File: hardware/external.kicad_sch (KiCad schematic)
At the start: 10 parts, among them J4 Conn_02x04_Odd_Even, J8 Conn_01x04_Pin, J9 Conn_01x04_Pin

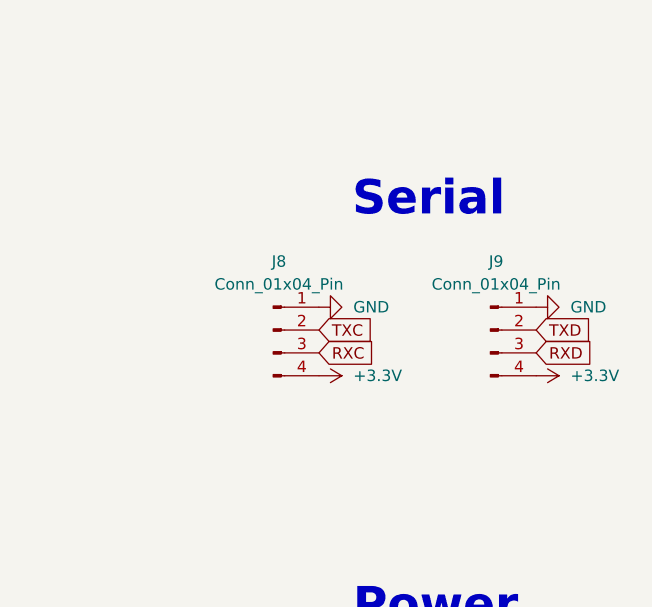
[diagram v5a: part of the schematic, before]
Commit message: Add new categories for Video&Audio and Sound System in project configuration
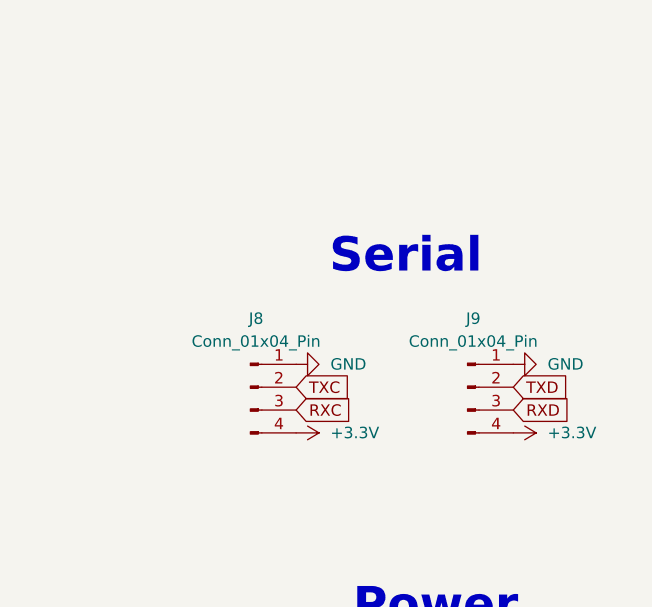
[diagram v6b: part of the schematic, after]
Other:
- moved on the sheet: J8, J9
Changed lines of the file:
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@@
 	(text "Serial\n"
 		(exclude_from_sim no)
-		(at 224.282 79.502 0)
+		(at 221.742 85.852 0)
 		(effects
 			(font
@@
 	(global_label "RXC"
 		(shape input)
-		(at 212.09 96.52 0)
+		(at 209.55 102.87 0)
 		(fields_autoplaced yes)
 		(effects
@@
 		)
 		(property "Intersheetrefs" "${INTERSHEET_REFS}"
-			(at 218.8247 96.52 0)
+			(at 216.2847 102.87 0)
 			(effects
 				(font
@@
 	(global_label "TXC"
 		(shape input)
-		(at 212.09 93.98 0)
+		(at 209.55 100.33 0)
 		(fields_autoplaced yes)
 		(effects
@@
 		)
 		(property "Intersheetrefs" "${INTERSHEET_REFS}"
-			(at 218.5223 93.98 0)
+			(at 215.9823 100.33 0)
 			(effects
 				(font
@@
 	(global_label "TXD"
 		(shape input)
-		(at 236.22 93.98 0)
+		(at 233.68 100.33 0)
 		(fields_autoplaced yes)
 		(effects
@@
 		)
 		(property "Intersheetrefs" "${INTERSHEET_REFS}"
-			(at 242.6523 93.98 0)
+			(at 240.1123 100.33 0)
 			(effects
 				(font
@@
 	(global_label "RXD"
 		(shape input)
-		(at 236.22 96.52 0)
+		(at 233.68 102.87 0)
 		(fields_autoplaced yes)
 		(effects
@@
 		)
 		(property "Intersheetrefs" "${INTERSHEET_REFS}"
-			(at 242.9547 96.52 0)
+			(at 240.4147 102.87 0)
 			(effects
 				(font
@@
 	(symbol
 		(lib_id "Connector:Conn_01x04_Pin")
-		(at 231.14 93.98 0)
+		(at 228.6 100.33 0)
 		(unit 1)
 		(exclude_from_sim no)
@@
 		(fields_autoplaced yes)
 		(property "Reference" "J9"
-			(at 231.775 86.36 0)
+			(at 229.235 92.71 0)
 			(effects
 				(font
@@
 		)
 		(property "Value" "Conn_01x04_Pin"
-			(at 231.775 88.9 0)
+			(at 229.235 95.25 0)
 			(effects
 				(font
@@
 		)
 		(property "Footprint" "Connector_PinHeader_2.54mm:PinHeader_1x04_P2.54mm_Vertical"
-			(at 231.14 93.98 0)
+			(at 228.6 100.33 0)
 			(effects
 				(font
@@
 		)
 		(property "Datasheet" "~"
-			(at 231.14 93.98 0)
+			(at 228.6 100.33 0)
 			(effects
 				(font
@@
 		)
 		(property "Description" "Generic connector, single row, 01x04, script generated"
-			(at 231.14 93.98 0)
+			(at 228.6 100.33 0)
 			(effects
 				(font
@@
 	(symbol
 		(lib_id "Connector:Conn_01x04_Pin")
-		(at 207.01 93.98 0)
+		(at 204.47 100.33 0)
 		(unit 1)
 		(exclude_from_sim no)
@@
 		(fields_autoplaced yes)
 		(property "Reference" "J8"
-			(at 207.645 86.36 0)
+			(at 205.105 92.71 0)
 			(effects
 				(font
@@
 		)
 		(property "Value" "Conn_01x04_Pin"
-			(at 207.645 88.9 0)
+			(at 205.105 95.25 0)
 			(effects
 				(font
@@
 		)
 		(property "Footprint" "Connector_PinHeader_2.54mm:PinHeader_1x04_P2.54mm_Vertical"
-			(at 207.01 93.98 0)
+			(at 204.47 100.33 0)
 			(effects
 				(font
@@
 		)
 		(property "Datasheet" "~"
-			(at 207.01 93.98 0)
+			(at 204.47 100.33 0)
 			(effects
 				(font
@@
 		)
 		(property "Description" "Generic connector, single row, 01x04, script generated"
-			(at 207.01 93.98 0)
+			(at 204.47 100.33 0)
 			(effects
 				(font
@@
 	(symbol
 		(lib_id "power:GND")
-		(at 212.09 91.44 90)
+		(at 209.55 97.79 90)
 		(unit 1)
 		(exclude_from_sim no)
@@
 		(fields_autoplaced yes)
 		(property "Reference" "#PWR0109"
-			(at 218.44 91.44 0)
+			(at 215.9 97.79 0)
 			(effects
 				(font
@@
 		)
 		(property "Value" "GND"
-			(at 215.9 91.4399 90)
+			(at 213.36 97.7899 90)
 			(effects
 				(font
@@
 		)
 		(property "Footprint" ""
-			(at 212.09 91.44 0)
+			(at 209.55 97.79 0)
 			(effects
 				(font
@@
 		)
 		(property "Datasheet" ""
-			(at 212.09 91.44 0)
+			(at 209.55 97.79 0)
 			(effects
 				(font
@@
 		)
 		(property "Description" "Power symbol creates a global label with name \"GND\" , ground"
-			(at 212.09 91.44 0)
+			(at 209.55 97.79 0)
 			(effects
 				(font
@@
 	(symbol
 		(lib_id "power:+3.3V")
-		(at 212.09 99.06 270)
+		(at 209.55 105.41 270)
 		(unit 1)
 		(exclude_from_sim no)
@@
 		(fields_autoplaced yes)
 		(property "Reference" "#PWR0110"
-			(at 208.28 99.06 0)
+			(at 205.74 105.41 0)
 			(effects
 				(font
@@
 		)
 		(property "Value" "+3.3V"
-			(at 215.9 99.0599 90)
+			(at 213.36 105.4099 90)
 			(effects
 				(font
@@
 		)
 		(property "Footprint" ""
-			(at 212.09 99.06 0)
+			(at 209.55 105.41 0)
 			(effects
 				(font
@@
 		)
 		(property "Datasheet" ""
-			(at 212.09 99.06 0)
+			(at 209.55 105.41 0)
 			(effects
 				(font
@@
 		)
 		(property "Description" "Power symbol creates a global label with name \"+3.3V\""
-			(at 212.09 99.06 0)
+			(at 209.55 105.41 0)
 			(effects
 				(font
@@
 	(symbol
 		(lib_id "power:+3.3V")
-		(at 236.22 99.06 270)
+		(at 233.68 105.41 270)
 		(unit 1)
 		(exclude_from_sim no)
@@
 		(fields_autoplaced yes)
 		(property "Reference" "#PWR0112"
-			(at 232.41 99.06 0)
+			(at 229.87 105.41 0)
 			(effects
 				(font
@@
 		)
 		(property "Value" "+3.3V"
-			(at 240.03 99.0599 90)
+			(at 237.49 105.4099 90)
 			(effects
 				(font
@@
 		)
 		(property "Footprint" ""
-			(at 236.22 99.06 0)
+			(at 233.68 105.41 0)
 			(effects
 				(font
@@
 		)
 		(property "Datasheet" ""
-			(at 236.22 99.06 0)
+			(at 233.68 105.41 0)
 			(effects
 				(font
@@
 		)
 		(property "Description" "Power symbol creates a global label with name \"+3.3V\""
-			(at 236.22 99.06 0)
+			(at 233.68 105.41 0)
 			(effects
 				(font
@@
 	(symbol
 		(lib_id "power:GND")
-		(at 236.22 91.44 90)
+		(at 233.68 97.79 90)
 		(unit 1)
 		(exclude_from_sim no)
@@
 		(fields_autoplaced yes)
 		(property "Reference" "#PWR0111"
-			(at 242.57 91.44 0)
+			(at 240.03 97.79 0)
 			(effects
 				(font
@@
 		)
 		(property "Value" "GND"
-			(at 240.03 91.4399 90)
+			(at 237.49 97.7899 90)
 			(effects
 				(font
@@
 		)
 		(property "Footprint" ""
-			(at 236.22 91.44 0)
+			(at 233.68 97.79 0)
 			(effects
 				(font
@@
 		)
 		(property "Datasheet" ""
-			(at 236.22 91.44 0)
+			(at 233.68 97.79 0)
 			(effects
 				(font
@@
 		)
 		(property "Description" "Power symbol creates a global label with name \"GND\" , ground"
-			(at 236.22 91.44 0)
+			(at 233.68 97.79 0)
 			(effects
 				(font

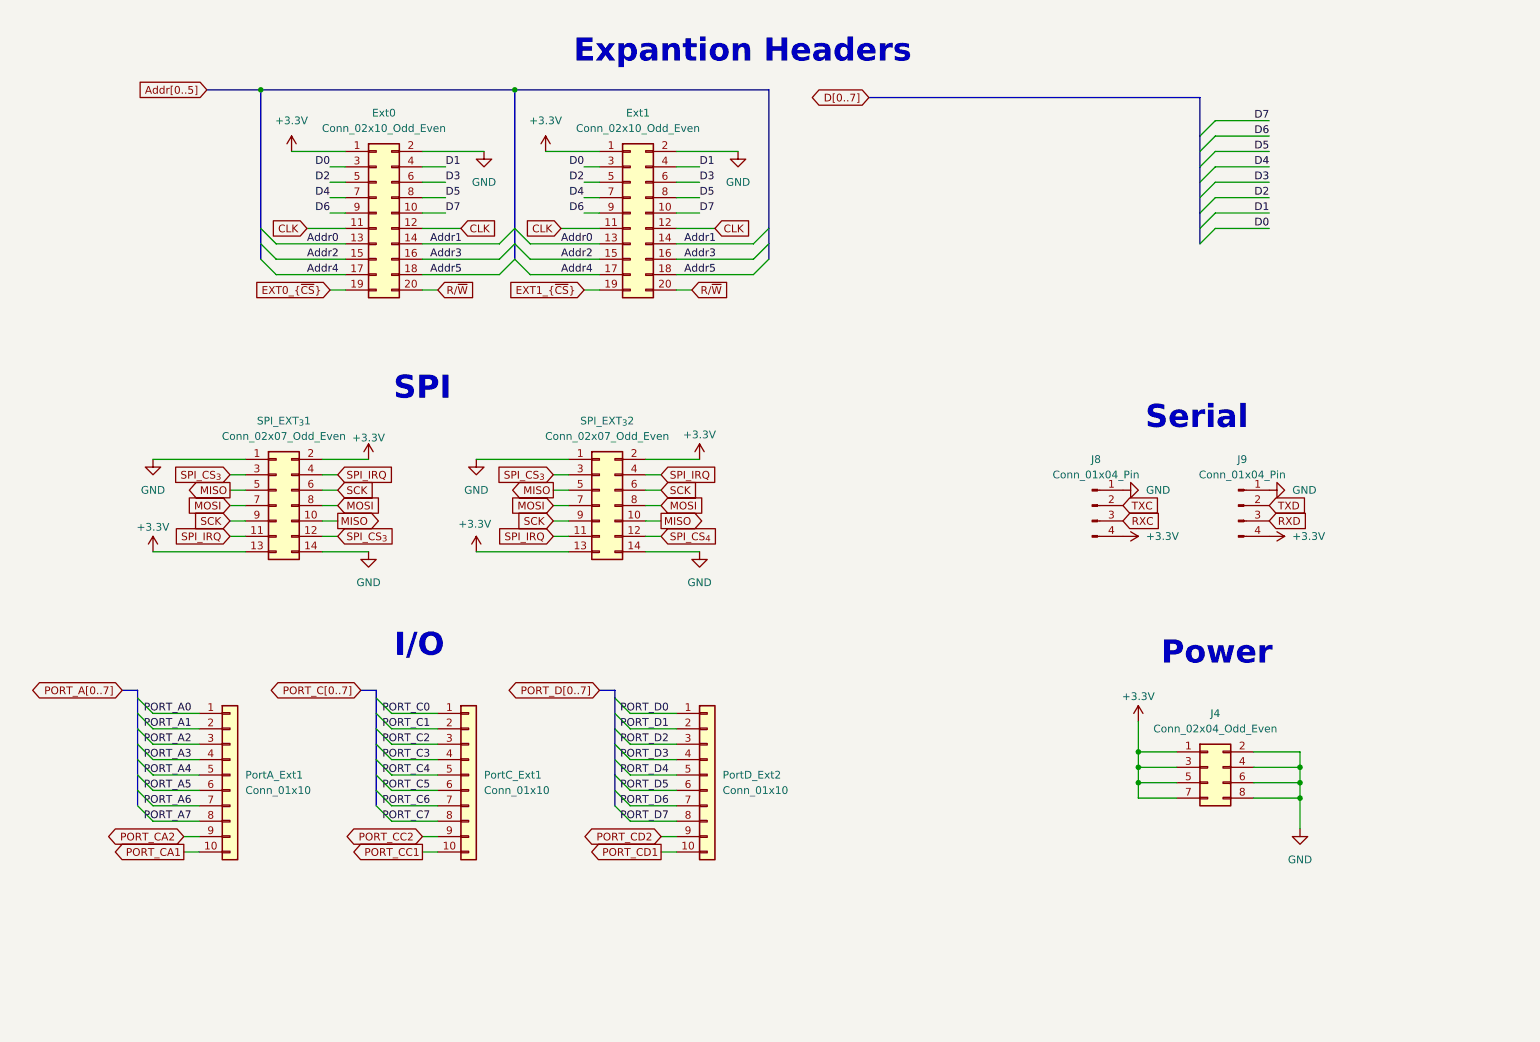
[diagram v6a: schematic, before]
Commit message: Moved connection to external connections
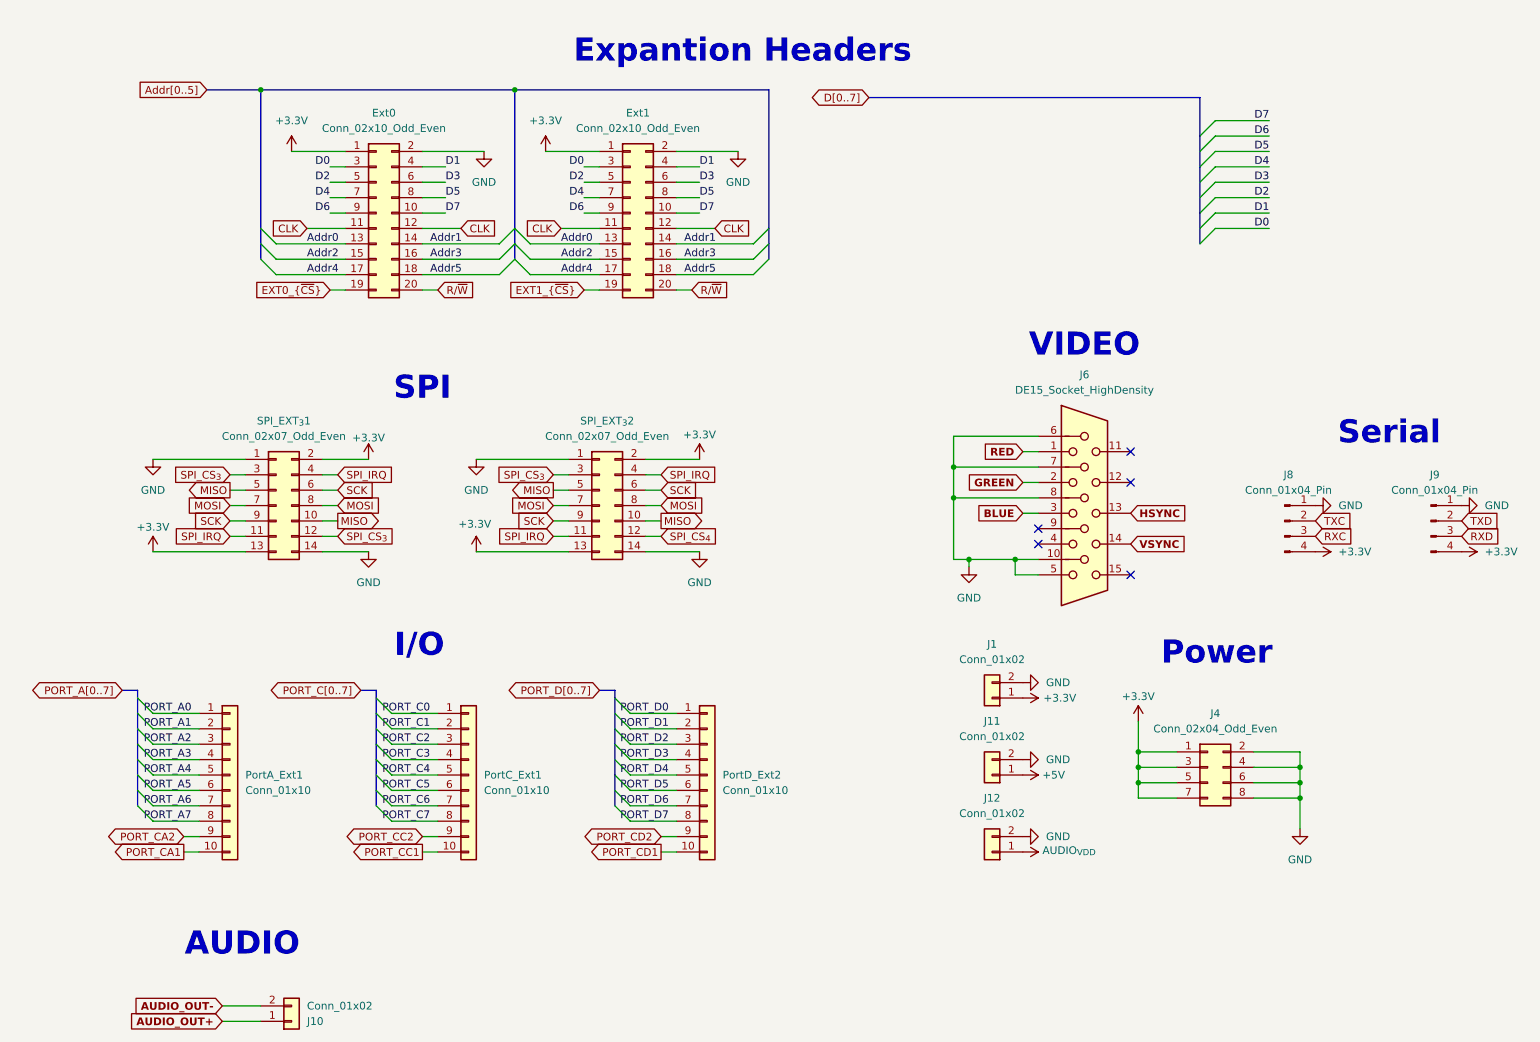
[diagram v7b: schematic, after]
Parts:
- added J1, J10, J11, J12: Conn_01x02, Connector_JST:JST_XH_B2B-XH-A_1x02_P2.50mm_Vertical, symbol Connector_Generic:Conn_01x02
- added J6: DE15_Socket_HighDensity, Connector_Dsub:DSUB-15_Socket_Horizontal_P2.77x2.84mm_EdgePinOffset9.40mm, symbol Connector:DE15_Socket_HighDensity
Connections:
- net +3.3V: now also J1.1 (Pin_1)
- net GND: now also J1.2 (Pin_2), J11.2 (Pin_2), J12.2 (Pin_2), J6.10, J6.5, J6.6, J6.7, J6.8
- new net +5V: J11.1 (Pin_1)
- new net AUDIO_OUT+: J10.1 (Pin_1)
- new net AUDIO_OUT-: J10.2 (Pin_2)
- new net AUDIO_{VDD}: J12.1 (Pin_1)
- new net BLUE: J6.3
- new net GREEN: J6.2
- new net HSYNC: J6.13
- new net RED: J6.1
- new net VSYNC: J6.14
- no-connect marks 0 -> 5
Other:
- note added: "AUDIO"
- note added: "VIDEO"
- moved on the sheet: J8, J9

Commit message: PCD DESIGN
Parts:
- renumbered J10 to AUDIO1, J4 to PWR_PIN1, J8 to SERIAL_C1, J9 to SERIAL_D1, J6 to VGA1
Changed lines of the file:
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@@
 		(dnp no)
 		(fields_autoplaced yes)
-		(property "Reference" "J9"
+		(property "Reference" "SERIAL_D1"
 			(at 260.985 95.25 0)
 			(effects
@@
 			(project "Lambda One"
 				(path "/73ea9964-373f-4fdc-b03e-f532cf836c0d/8596ee45-8820-47ce-a360-877e286ae437"
-					(reference "J9")
+					(reference "SERIAL_D1")
 					(unit 1)
 				)
@@
 		(dnp no)
 		(fields_autoplaced yes)
-		(property "Reference" "J8"
+		(property "Reference" "SERIAL_C1"
 			(at 236.855 95.25 0)
 			(effects
@@
 			(project "Lambda One"
 				(path "/73ea9964-373f-4fdc-b03e-f532cf836c0d/8596ee45-8820-47ce-a360-877e286ae437"
-					(reference "J8")
+					(reference "SERIAL_C1")
 					(unit 1)
 				)
@@
 		(on_board yes)
 		(dnp no)
-		(property "Reference" "J10"
+		(property "Reference" "AUDIO1"
 			(at 74.93 185.4201 0)
 			(effects
@@
 			(project "Lambda One"
 				(path "/73ea9964-373f-4fdc-b03e-f532cf836c0d/8596ee45-8820-47ce-a360-877e286ae437"
-					(reference "J10")
+					(reference "AUDIO1")
 					(unit 1)
 				)
@@
 		(dnp no)
 		(fields_autoplaced yes)
-		(property "Reference" "J6"
+		(property "Reference" "VGA1"
 			(at 203.2 78.74 0)
 			(effects
@@
 			(project "Lambda One"
 				(path "/73ea9964-373f-4fdc-b03e-f532cf836c0d/8596ee45-8820-47ce-a360-877e286ae437"
-					(reference "J6")
+					(reference "VGA1")
 					(unit 1)
 				)
@@
 		(dnp no)
 		(fields_autoplaced yes)
-		(property "Reference" "J4"
+		(property "Reference" "PWR_PIN1"
 			(at 224.79 134.62 0)
 			(effects
@@
 			(project "Lambda One"
 				(path "/73ea9964-373f-4fdc-b03e-f532cf836c0d/8596ee45-8820-47ce-a360-877e286ae437"
-					(reference "J4")
-					(unit 1)
-				)
+					(reference "PWR_PIN1")
+					(unit 1)
+				)
